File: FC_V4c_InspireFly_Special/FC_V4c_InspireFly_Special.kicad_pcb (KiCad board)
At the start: 4 copper layers, 88 x 94.5 mm, 155 parts, among them IC1 RP2040_QFN56, IC2 AZ1117CH-3.3TRG1, IC3 RV-3028-C7_32.768kHz_1ppm_TA_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, J1 Conn_ARM_JTAG_SWD_10, J10 Breakout, J11 Breakout, J12 BM04B-SRSS-TB(LF)(SN), J13 Breakout, J14 Battery, J15 Breakout, J16 Debug, J2 FC to EPS Connector, J3 Life Makes Lemonade, J4 Molex 503398-1892, J5 BM04B-SRSS-TB(LF)(SN), J6 Conn_Coaxial, J7 Breakout, J8 USB_B_Micro, J9 BM04B-SRSS-TB(LF)(SN), SW1 KMR2, SW2 KMR2, U1 TLV1704, U10 AP3602AKTR-G1, U4 RFM98PW, U5 RFM9xBreakout, U6 W25Q128JV, U7 LSM6DSOTR, U8 LSM303AGRTR, U9 MCP25625-E/ML, Y1 12MHZ, Y3 16MHZ 12 pf

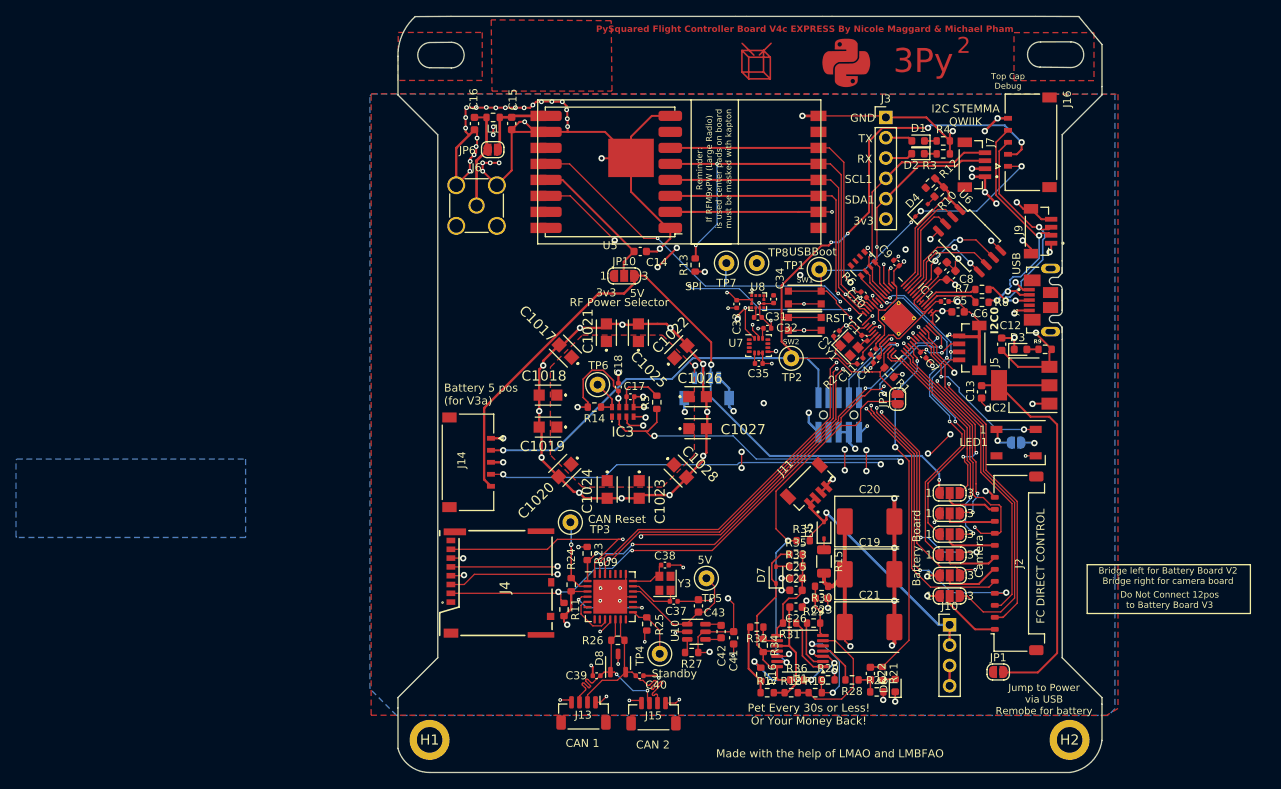
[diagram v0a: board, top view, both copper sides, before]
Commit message: Added Jumper for 5V V_RF Bias
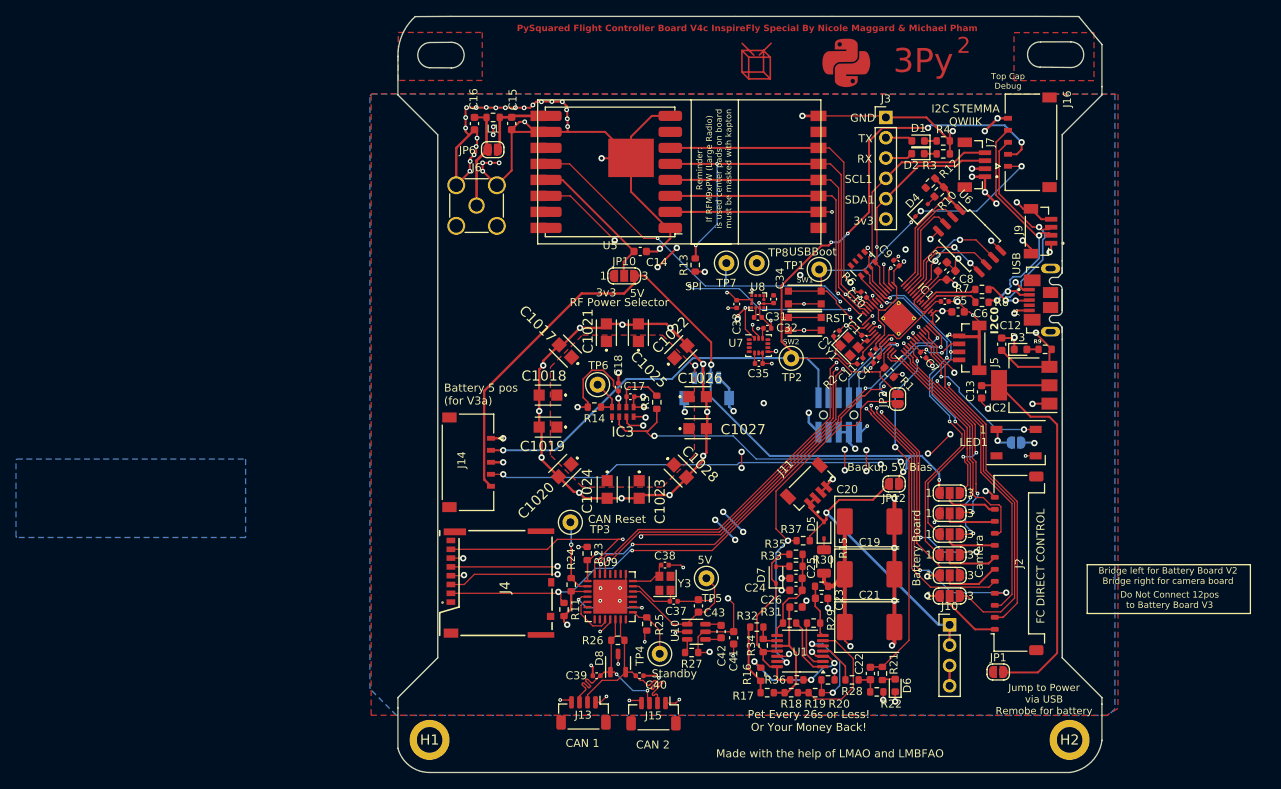
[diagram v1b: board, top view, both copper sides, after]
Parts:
- removed the G*** at (162.2, 52.5)
- added JP12: SolderJumper_2_Open, Jumper:SolderJumper-2_P1.3mm_Open_RoundedPad1.0x1.5mm, F.Cu at (205.3, 106.0)
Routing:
- net VBATT: track 32.1 -> 42.0 mm
- net 3.3V: track 108.7 -> 115.8 mm, vias 35 -> 39
- net VCC_RF1: track 91.2 -> 96.6 mm, vias 2 -> 3
- net D7: track 33.8 -> 31.0 mm, vias 1 -> 0
- net VBUS_RESET / D4: track 40.7 -> 38.0 mm, vias 3 -> 2
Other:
- board text added: "Backup 5V Bias"
- board text added: "Pet Every 26s or Less! Or Your Money Back!"
- board text added: "PySquared Flight Controller Board V4c InspireFly Special By Nicole Maggard & Michael Pham"
- board text removed: "Pet Every 30s or Less! Or Your Money Back!"
- board text removed: "PySquared Flight Controller Board V4c EXPRESS By Nicole Maggard & Michael Pham"

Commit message: Finished InspireFly Special
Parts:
- removed C15, C16: DNI, Capacitor_SMD:C_0603_1608Metric
- removed JP6: SolderJumper_2_Open, Jumper:SolderJumper-2_P1.3mm_Open_RoundedPad1.0x1.5mm
- removed L1: DNI, Resistor_SMD:R_0603_1608Metric
- G***: moved to F.Cu
- moved G*** 80.5 mm to (171.0, 53.0), turned to 0 degrees
- moved J6 2.39 mm to (153.2, 73.6)
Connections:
- J6 pad 1: Net-(J6-In) -> RF1_ANT
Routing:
- net Net-(J6-In): track 13.3 -> 0.00 mm
- net RF1_ANT: track 10.5 -> 20.1 mm
- net SPI0_MISO: track 114.8 -> 111.7 mm
- net /WDT-VIN: track 40.7 -> 39.1 mm, vias 5 -> 4
- net RF1_IO0: track 66.3 -> 64.9 mm
- net GND: track 359.9 -> 358.5 mm, vias 115 -> 121
- net RF1_IO4: track 61.3 -> 59.9 mm
- net SPI0_SCK: track 114.5 -> 113.5 mm
- net /WDT-VP: track 13.9 -> 13.2 mm
- net /3v3 Spec: track 54.6 -> 54.0 mm
- net VBATT: track 42.0 -> 41.4 mm
- removed copper zone on B.Cu, net (none)
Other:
- board text added: "JLCJLCJLCJLC"
- board text removed: "BRONCO SPACE Educational Product For Instructional Use Only"
- board text removed: "Do Not Connect 12pos to Battery Board V3"
